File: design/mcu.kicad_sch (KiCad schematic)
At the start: 30 parts, among them J2 SWD_01X04, J3 DEBUG_SPI, U6 STM32H750VBTx, X1 ASTX-H11-25.000MHZ-T

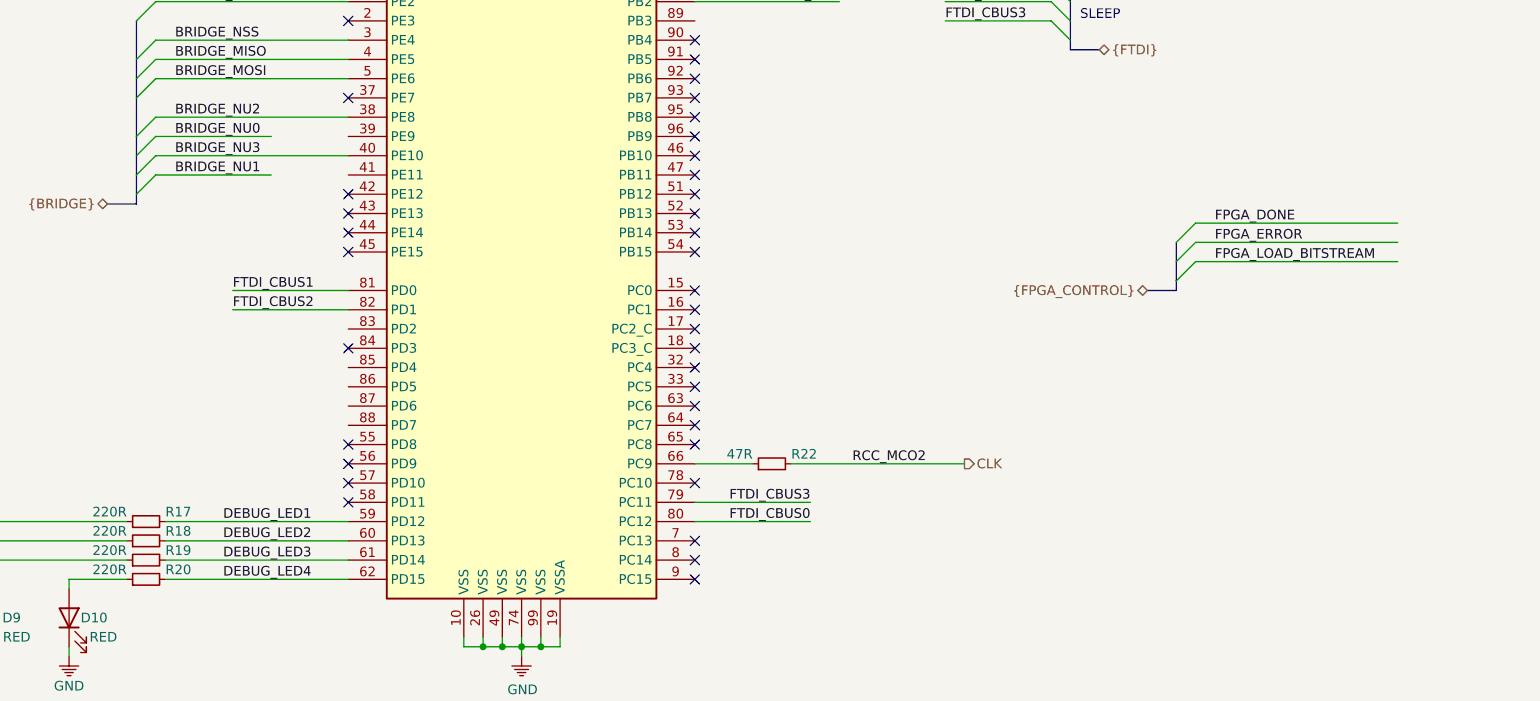
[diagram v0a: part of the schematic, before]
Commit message: Connected FPGA controll
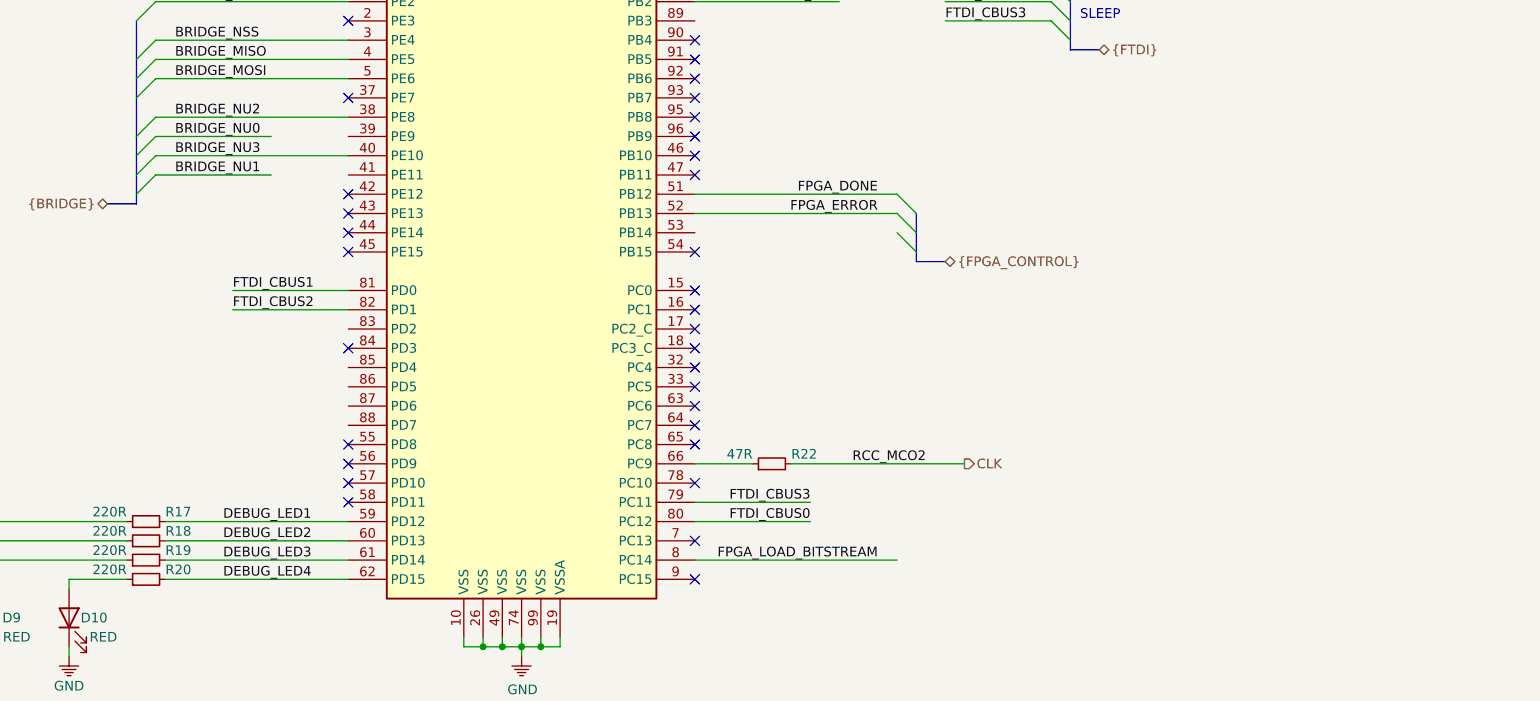
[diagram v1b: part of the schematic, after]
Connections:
- net FPGA_DONE: now also U6.51 (PB12)
- net FPGA_ERROR: now also U6.52 (PB13)
- net FPGA_LOAD_BITSTREAM: now also U6.8 (PC14)
- no-connect marks 49 -> 45
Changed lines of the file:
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@@
   (no_connect (at 123.19 109.22))
   (no_connect (at 168.91 101.6))
-  (no_connect (at 168.91 127))
   (no_connect (at 168.91 142.24))
   (no_connect (at 168.91 55.88))
@@
   (no_connect (at 168.91 144.78))
   (no_connect (at 168.91 137.16))
-  (no_connect (at 168.91 124.46))
   (no_connect (at 168.91 116.84))
-  (no_connect (at 168.91 121.92))
   (no_connect (at 168.91 104.14))
-  (no_connect (at 168.91 170.18))
   (bus_entry (at 95.25 99.06) (size 2.54 -2.54))
   (bus_entry (at 95.25 104.14) (size 2.54 -2.54))
@@
   (bus_entry (at 95.25 119.38) (size 2.54 -2.54))
   (bus_entry (at 95.25 121.92) (size 2.54 -2.54))
+  (bus_entry (at 198.12 124.46) (size -2.54 -2.54))
+  (bus_entry (at 198.12 127) (size -2.54 -2.54))
+  (bus_entry (at 198.12 129.54) (size -2.54 -2.54))
   (bus_entry (at 218.44 73.66) (size -2.54 -2.54))
   (bus_entry (at 218.44 76.2) (size -2.54 -2.54))
@@
   (bus_entry (at 218.44 99.06) (size -2.54 -2.54))
   (bus_entry (at 218.44 101.6) (size -2.54 -2.54))
-  (bus_entry (at 232.41 128.27) (size 2.54 -2.54))
-  (bus_entry (at 232.41 130.81) (size 2.54 -2.54))
-  (bus_entry (at 232.41 133.35) (size 2.54 -2.54))
   (wire (pts (xy 20.32 22.86) (xy 20.32 24.13)))
   (wire (pts (xy 20.32 24.13) (xy 30.48 24.13)))
@@
   (wire (pts (xy 190.5 25.4) (xy 201.93 25.4)))
   (wire (pts (xy 190.5 34.29) (xy 190.5 35.56)))
+  (wire (pts (xy 195.58 121.92) (xy 168.91 121.92)))
+  (wire (pts (xy 195.58 124.46) (xy 168.91 124.46)))
+  (wire (pts (xy 195.58 170.18) (xy 168.91 170.18)))
   (wire (pts (xy 201.93 25.4) (xy 201.93 26.67)))
   (wire (pts (xy 201.93 25.4) (xy 213.36 25.4)))
@@
   (wire (pts (xy 224.79 25.4) (xy 236.22 25.4)))
   (wire (pts (xy 224.79 35.56) (xy 224.79 36.83)))
-  (wire (pts (xy 234.95 125.73) (xy 261.62 125.73)))
-  (wire (pts (xy 234.95 128.27) (xy 261.62 128.27)))
-  (wire (pts (xy 234.95 130.81) (xy 261.62 130.81)))
   (wire (pts (xy 236.22 25.4) (xy 236.22 27.94)))
   (wire (pts (xy 236.22 25.4) (xy 247.65 25.4)))
@@
   (bus (pts (xy 95.25 99.06) (xy 95.25 106.68)))
   (bus (pts (xy 95.25 106.68) (xy 95.25 114.3)))
-  (bus (pts (xy 95.25 114.3) (xy 95.25 119.38)))
-  (bus (pts (xy 95.25 119.38) (xy 95.25 123.19)))
+  (bus (pts (xy 95.25 114.3) (xy 95.25 116.84)))
+  (bus (pts (xy 95.25 116.84) (xy 95.25 121.92)))
+  (bus (pts (xy 95.25 121.92) (xy 95.25 123.19)))
+  (bus (pts (xy 198.12 124.46) (xy 198.12 127)))
+  (bus (pts (xy 198.12 127) (xy 198.12 130.81)))
+  (bus (pts (xy 201.93 130.81) (xy 198.12 130.81)))
   (bus (pts (xy 218.44 73.66) (xy 218.44 78.74)))
   (bus (pts (xy 218.44 78.74) (xy 218.44 93.98)))
@@
   (bus (pts (xy 218.44 99.06) (xy 218.44 102.87)))
   (bus (pts (xy 218.44 102.87) (xy 222.25 102.87)))
-  (bus (pts (xy 228.6 134.62) (xy 232.41 134.62)))
-  (bus (pts (xy 232.41 128.27) (xy 232.41 133.35)))
-  (bus (pts (xy 232.41 133.35) (xy 232.41 134.62)))
   (polyline (pts (xy 186.69 13.97) (xy 186.69 44.45)))
   (polyline (pts (xy 186.69 13.97) (xy 256.54 13.97)))
@@
     (effects (font (size 1.27 1.27)) (justify right bottom))
   )
+  (label "FPGA_DONE" (at 193.04 121.92 180)
+    (effects (font (size 1.27 1.27)) (justify right bottom))
+  )
+  (label "FPGA_ERROR" (at 193.04 124.46 180)
+    (effects (font (size 1.27 1.27)) (justify right bottom))
+  )
+  (label "FPGA_LOAD_BITSTREAM" (at 193.04 170.18 180)
+    (effects (font (size 1.27 1.27)) (justify right bottom))
+  )
   (label "RCC_MCO2" (at 199.39 157.48 180)
     (effects (font (size 1.27 1.27)) (justify right bottom))
@@
   )
   (label "FTDI_CBUS3" (at 201.93 99.06 0)
-    (effects (font (size 1.27 1.27)) (justify left bottom))
-  )
-  (label "FPGA_DONE" (at 237.49 125.73 0)
-    (effects (font (size 1.27 1.27)) (justify left bottom))
-  )
-  (label "FPGA_ERROR" (at 237.49 128.27 0)
-    (effects (font (size 1.27 1.27)) (justify left bottom))
-  )
-  (label "FPGA_LOAD_BITSTREAM" (at 237.49 130.81 0)
     (effects (font (size 1.27 1.27)) (justify left bottom))
   )
@@
     (effects (font (size 1.27 1.27)) (justify right))
   )
+  (hierarchical_label "{FPGA_CONTROL}" (shape bidirectional) (at 201.93 130.81 0)
+    (effects (font (size 1.27 1.27)) (justify left))
+  )
   (hierarchical_label "CLK" (shape output) (at 204.47 157.48 0)
     (effects (font (size 1.27 1.27)) (justify left))
@@
     (effects (font (size 1.27 1.27)) (justify left))
   )
-  (hierarchical_label "{FPGA_CONTROL}" (shape bidirectional) (at 228.6 134.62 180)
-    (effects (font (size 1.27 1.27)) (justify right))
-  )
   (symbol (lib_id "KLIB_Power:PWR_FLAG") (at 83.82 58.42 90) (unit 1)

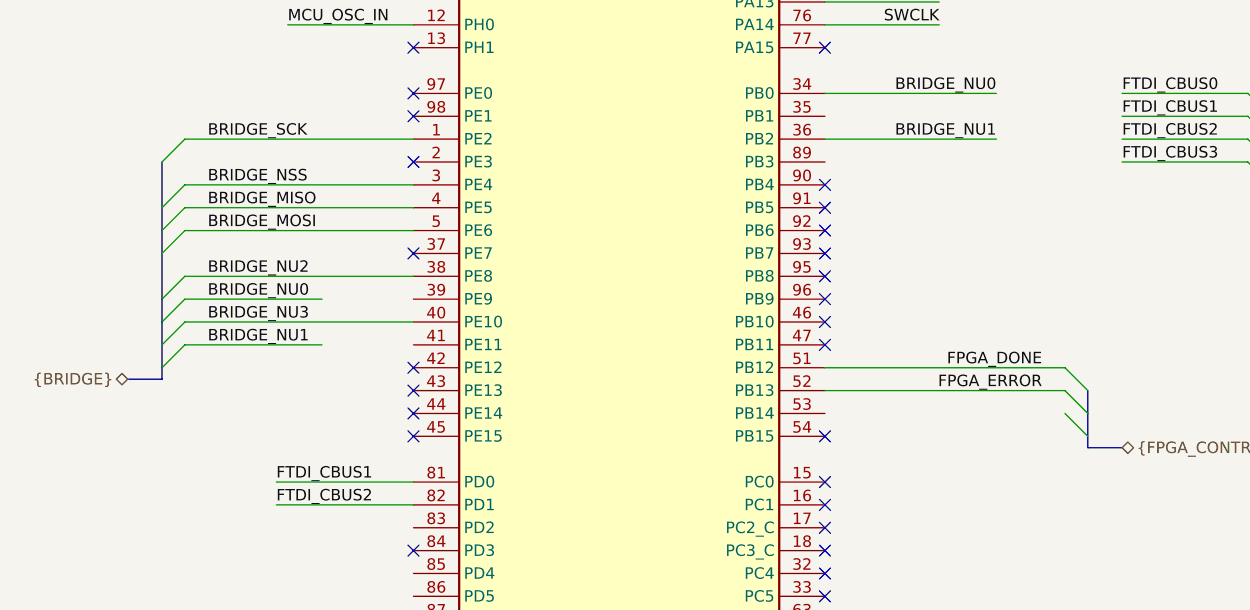
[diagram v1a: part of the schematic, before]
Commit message: Refactored FPGA schematic
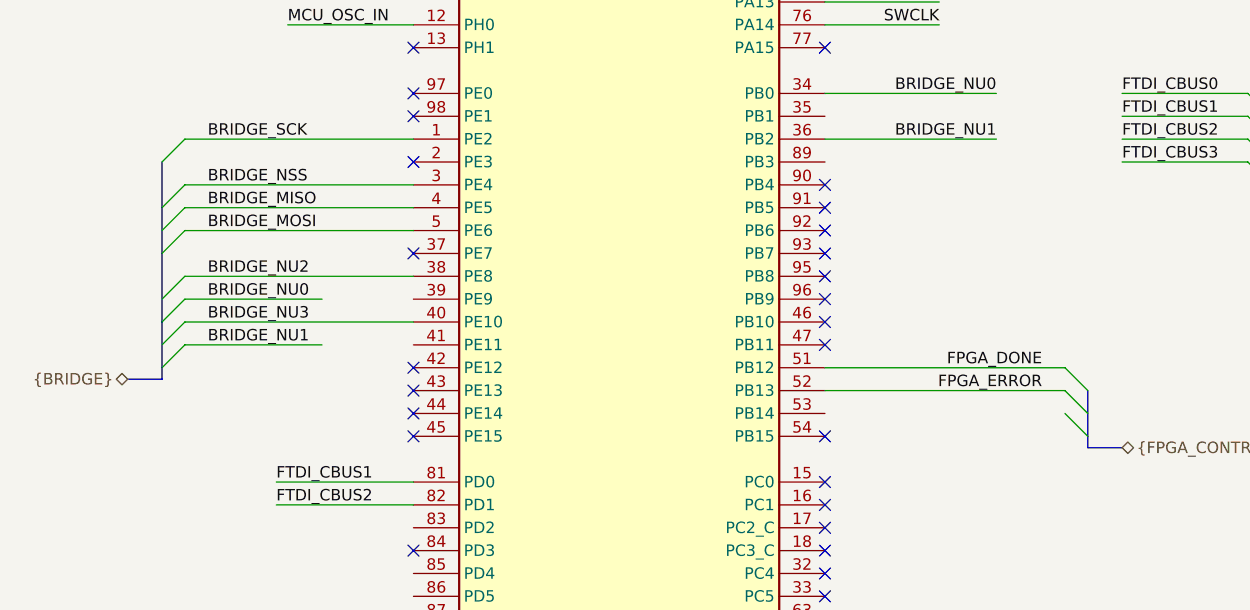
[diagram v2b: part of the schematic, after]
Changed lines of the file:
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@@
-(kicad_sch (version 20200512) (host eeschema "5.99.0-unknown-ad88874~101~ubuntu18.04.1")
-  (page 3 8)
+(kicad_sch (version 20200512) (host eeschema "5.99.0-unknown-92ce7ca~101~ubuntu18.04.1")
+  (page 1 8)
   (paper "A4")
   (title_block
@@
   (junction (at 236.22 25.4))
   (junction (at 262.89 26.67))
-  (no_connect (at 123.19 99.06))
-  (no_connect (at 168.91 63.5))
-  (no_connect (at 168.91 134.62))
-  (no_connect (at 168.91 106.68))
+  (no_connect (at 168.91 116.84))
+  (no_connect (at 168.91 167.64))
+  (no_connect (at 168.91 129.54))
+  (no_connect (at 168.91 149.86))
   (no_connect (at 168.91 152.4))
-  (no_connect (at 123.19 157.48))
-  (no_connect (at 123.19 86.36))
-  (no_connect (at 123.19 127))
-  (no_connect (at 168.91 58.42))
-  (no_connect (at 168.91 154.94))
-  (no_connect (at 123.19 124.46))
+  (no_connect (at 168.91 142.24))
+  (no_connect (at 168.91 66.04))
   (no_connect (at 168.91 114.3))
-  (no_connect (at 123.19 154.94))
-  (no_connect (at 168.91 147.32))
-  (no_connect (at 168.91 66.04))
-  (no_connect (at 123.19 160.02))
+  (no_connect (at 123.19 162.56))
   (no_connect (at 168.91 160.02))
-  (no_connect (at 168.91 129.54))
-  (no_connect (at 168.91 86.36))
-  (no_connect (at 123.19 93.98))
-  (no_connect (at 168.91 111.76))
-  (no_connect (at 168.91 109.22))
-  (no_connect (at 123.19 162.56))
-  (no_connect (at 168.91 53.34))
-  (no_connect (at 168.91 119.38))
-  (no_connect (at 168.91 149.86))
-  (no_connect (at 123.19 121.92))
-  (no_connect (at 123.19 142.24))
-  (no_connect (at 168.91 50.8))
-  (no_connect (at 168.91 68.58))
-  (no_connect (at 123.19 129.54))
+  (no_connect (at 123.19 91.44))
   (no_connect (at 168.91 172.72))
-  (no_connect (at 168.91 167.64))
-  (no_connect (at 168.91 48.26))
-  (no_connect (at 123.19 91.44))
-  (no_connect (at 168.91 60.96))
-  (no_connect (at 123.19 109.22))
-  (no_connect (at 168.91 101.6))
-  (no_connect (at 168.91 142.24))
-  (no_connect (at 168.91 55.88))
-  (no_connect (at 168.91 139.7))
   (no_connect (at 168.91 144.78))
   (no_connect (at 168.91 137.16))
-  (no_connect (at 168.91 116.84))
+  (no_connect (at 168.91 86.36))
+  (no_connect (at 123.19 127))
+  (no_connect (at 168.91 50.8))
+  (no_connect (at 168.91 48.26))
+  (no_connect (at 168.91 154.94))
+  (no_connect (at 168.91 111.76))
   (no_connect (at 168.91 104.14))
+  (no_connect (at 168.91 60.96))
+  (no_connect (at 168.91 147.32))
+  (no_connect (at 123.19 93.98))
+  (no_connect (at 168.91 106.68))
+  (no_connect (at 123.19 99.06))
+  (no_connect (at 123.19 129.54))
+  (no_connect (at 168.91 139.7))
+  (no_connect (at 123.19 154.94))
+  (no_connect (at 168.91 119.38))
+  (no_connect (at 168.91 109.22))
+  (no_connect (at 168.91 134.62))
+  (no_connect (at 168.91 55.88))
+  (no_connect (at 168.91 101.6))
+  (no_connect (at 123.19 160.02))
+  (no_connect (at 123.19 157.48))
+  (no_connect (at 123.19 121.92))
+  (no_connect (at 168.91 63.5))
+  (no_connect (at 123.19 86.36))
+  (no_connect (at 168.91 53.34))
+  (no_connect (at 168.91 58.42))
+  (no_connect (at 168.91 68.58))
+  (no_connect (at 123.19 109.22))
+  (no_connect (at 123.19 142.24))
+  (no_connect (at 123.19 124.46))
   (bus_entry (at 95.25 99.06) (size 2.54 -2.54))
   (bus_entry (at 95.25 104.14) (size 2.54 -2.54))
@@
   (wire (pts (xy 274.32 35.56) (xy 274.32 36.83)))
   (bus (pts (xy 91.44 123.19) (xy 95.25 123.19)))
-  (bus (pts (xy 95.25 99.06) (xy 95.25 106.68)))
-  (bus (pts (xy 95.25 106.68) (xy 95.25 114.3)))
-  (bus (pts (xy 95.25 114.3) (xy 95.25 116.84)))
+  (bus (pts (xy 95.25 99.06) (xy 95.25 104.14)))
+  (bus (pts (xy 95.25 104.14) (xy 95.25 109.22)))
+  (bus (pts (xy 95.25 109.22) (xy 95.25 116.84)))
   (bus (pts (xy 95.25 116.84) (xy 95.25 121.92)))
   (bus (pts (xy 95.25 121.92) (xy 95.25 123.19)))
-  (bus (pts (xy 198.12 124.46) (xy 198.12 127)))
-  (bus (pts (xy 198.12 127) (xy 198.12 130.81)))
+  (bus (pts (xy 198.12 124.46) (xy 198.12 129.54)))
+  (bus (pts (xy 198.12 129.54) (xy 198.12 130.81)))
   (bus (pts (xy 201.93 130.81) (xy 198.12 130.81)))
   (bus (pts (xy 218.44 73.66) (xy 218.44 78.74)))
